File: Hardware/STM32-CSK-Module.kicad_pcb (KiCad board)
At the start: 2 copper layers, 32 parts, among them J1 Conn_Cortex-JTAG-10, U1 STM32F417VGT, X1 8MHz, X2 32.768kHz

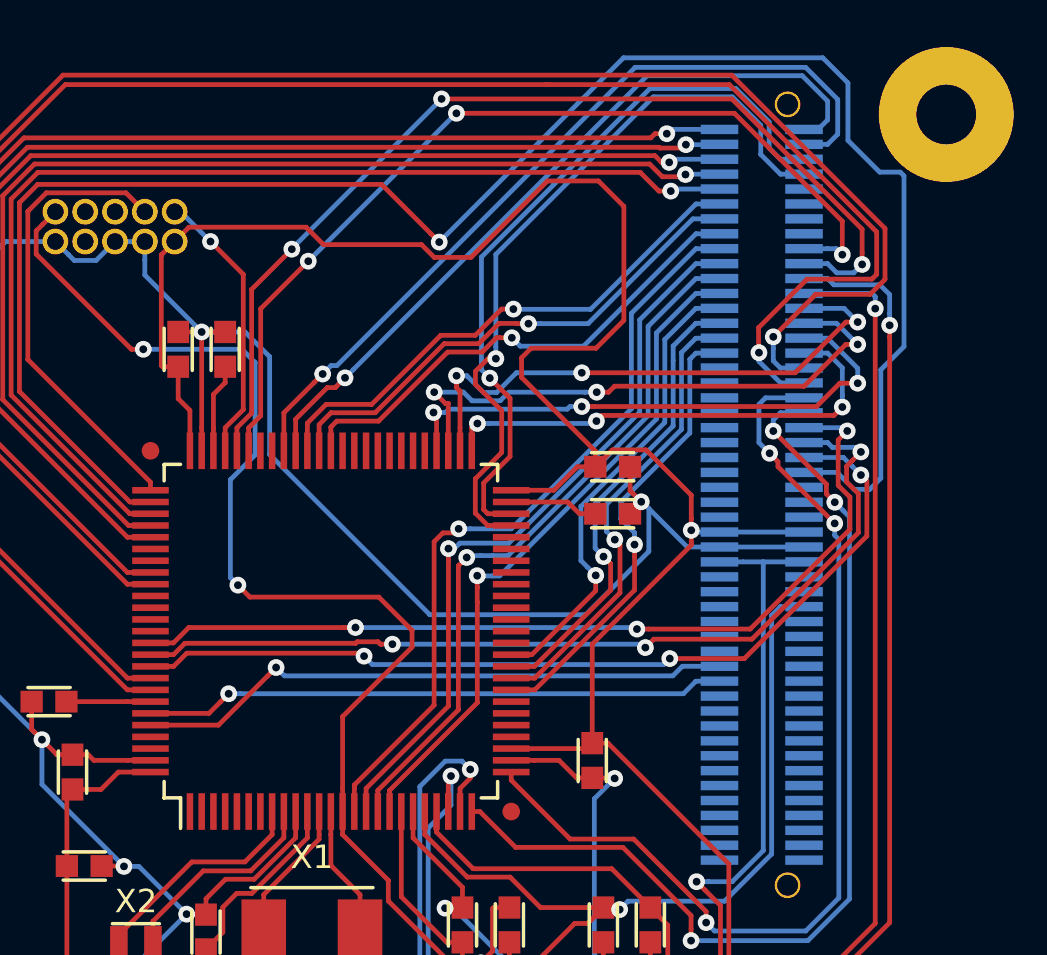
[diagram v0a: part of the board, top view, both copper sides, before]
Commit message: Finished all H1 GPIO
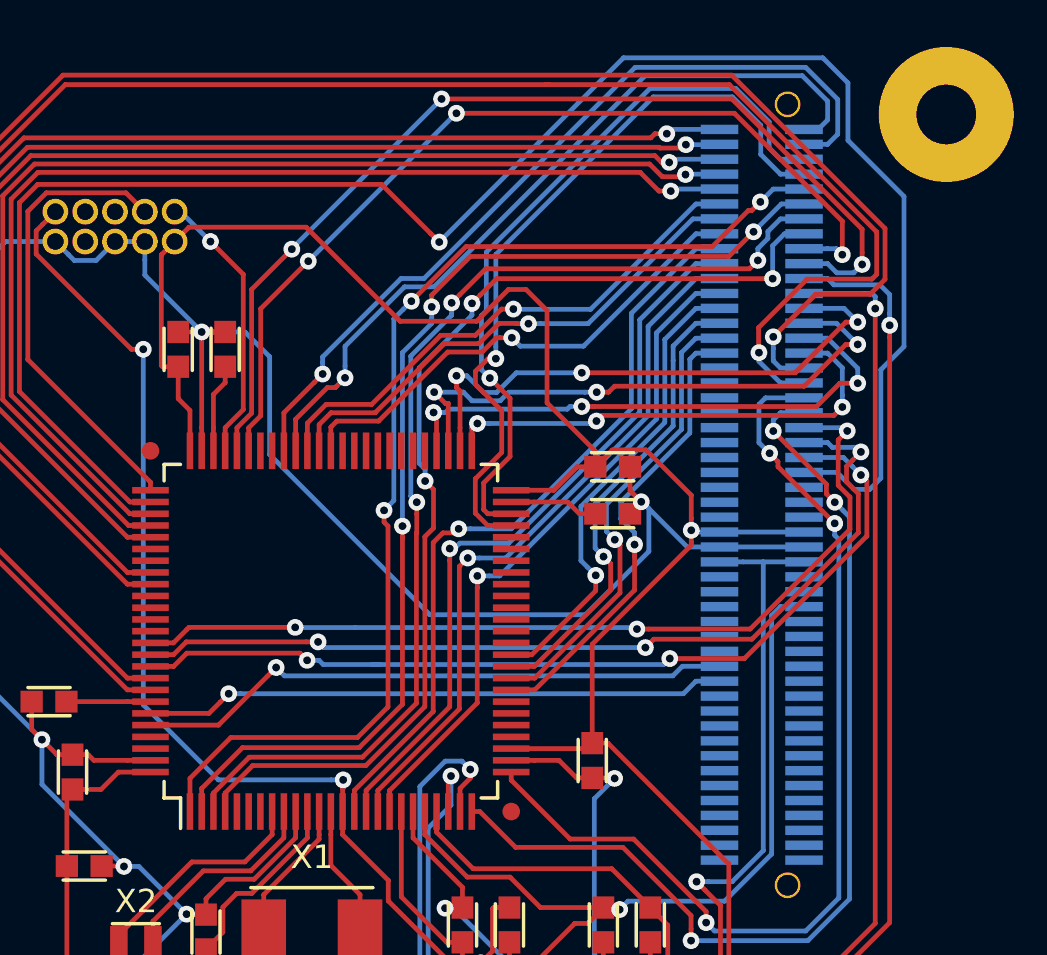
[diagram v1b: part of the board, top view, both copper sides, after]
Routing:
- net /IO19: track 0.00 -> 47.6 mm, vias 0 -> 3
- net /IO18: track 0.00 -> 46.4 mm, vias 0 -> 3
- net /IO17: track 0.00 -> 45.9 mm, vias 0 -> 3
- net /IO16: track 0.00 -> 45.5 mm, vias 0 -> 3
- net +3V3: track 159.9 -> 148.6 mm
- net /~RST: track 53.8 -> 48.0 mm
- net /I2C3_SDA: track 32.5 -> 33.3 mm
- net /~SPI1_SS: track 78.4 -> 77.9 mm

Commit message: Done. Moderately clean.
All used pins routed.
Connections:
- H1 pad 33: Net-(H1-Pad33) -> /IO31
- H1 pad 35: Net-(H1-Pad35) -> /IO30
- H1 pad 37: Net-(H1-Pad37) -> /IO29
- H1 pad 39: Net-(H1-Pad39) -> /IO28
- H1 pad 41: Net-(H1-Pad41) -> /IO27
- H1 pad 43: Net-(H1-Pad43) -> /IO26
- H1 pad 45: Net-(H1-Pad45) -> /IO25
- H1 pad 47: Net-(H1-Pad47) -> /IO24
- U1 pad 29: Net-(U1-Pad29) -> /IO28
- U1 pad 30: Net-(U1-Pad30) -> /IO29
- U1 pad 31: Net-(U1-Pad31) -> /IO30
- U1 pad 32: Net-(U1-Pad32) -> /IO31
- U1 pad 68: Net-(U1-Pad68) -> /IO27
- U1 pad 69: Net-(U1-Pad69) -> /IO26
- U1 pad 97: Net-(U1-Pad97) -> /IO24
- U1 pad 98: Net-(U1-Pad98) -> /IO25
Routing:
- net /IO26: track 0.00 -> 43.4 mm, vias 0 -> 3
- net /IO27: track 0.00 -> 40.5 mm, vias 0 -> 3
- net /IO25: track 0.00 -> 39.2 mm, vias 0 -> 3
- net /IO24: track 0.00 -> 37.0 mm, vias 0 -> 3
- net /IO28: track 0.00 -> 19.5 mm, vias 0 -> 1
- net /IO30: track 0.00 -> 19.4 mm, vias 0 -> 1
- net /IO31: track 0.00 -> 19.4 mm, vias 0 -> 1
- net /IO29: track 0.00 -> 19.0 mm, vias 0 -> 1
- net /SPI1_SCK: track 38.3 -> 46.8 mm
- net /SPI1_MISO: track 39.0 -> 46.5 mm
- net /SPI1_MOSI: track 38.9 -> 46.2 mm
- net +3V3: track 148.6 -> 151.1 mm
- net /USART1_RX: track 80.0 -> 82.2 mm
- net /USART1_TX: track 79.7 -> 81.4 mm
- net /~SPI1_SS: track 77.9 -> 79.4 mm
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
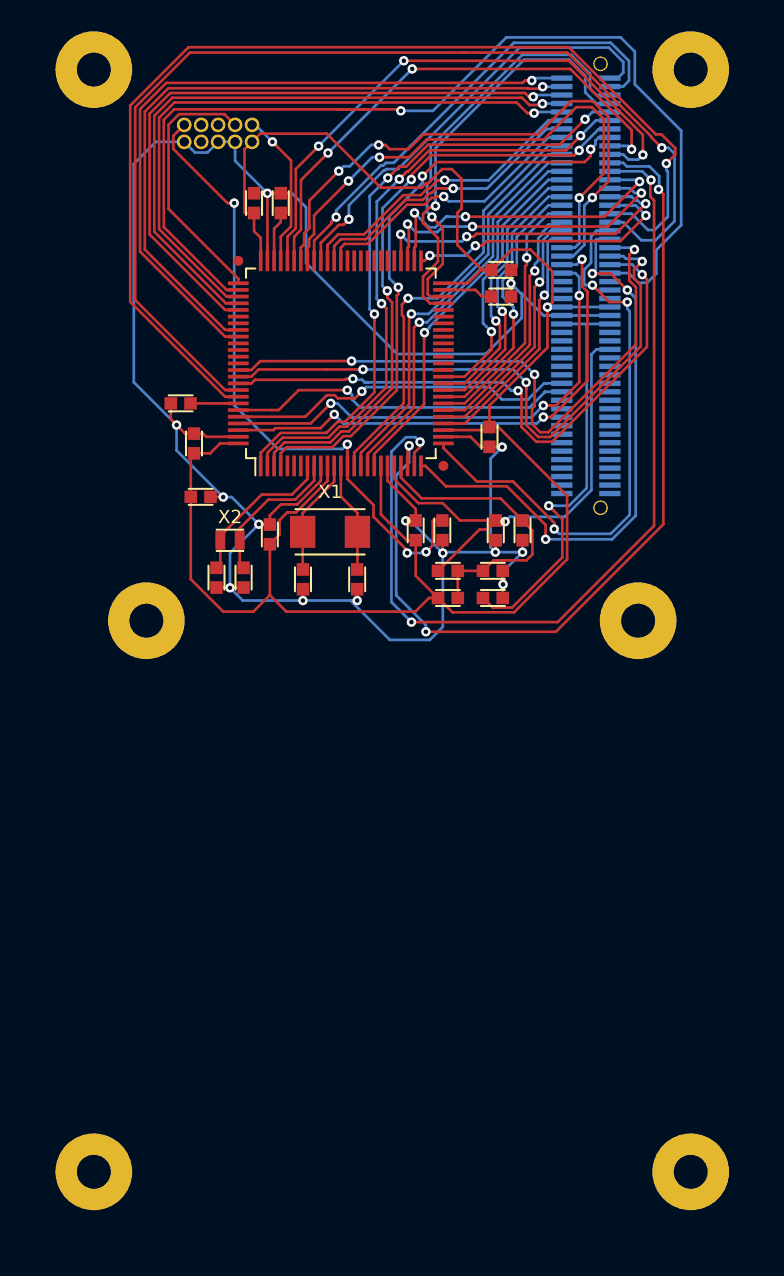
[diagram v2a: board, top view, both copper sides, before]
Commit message: Created ground plane
Large parts of ground plane unconnected. Not surprising given the density
of traces in most parts.
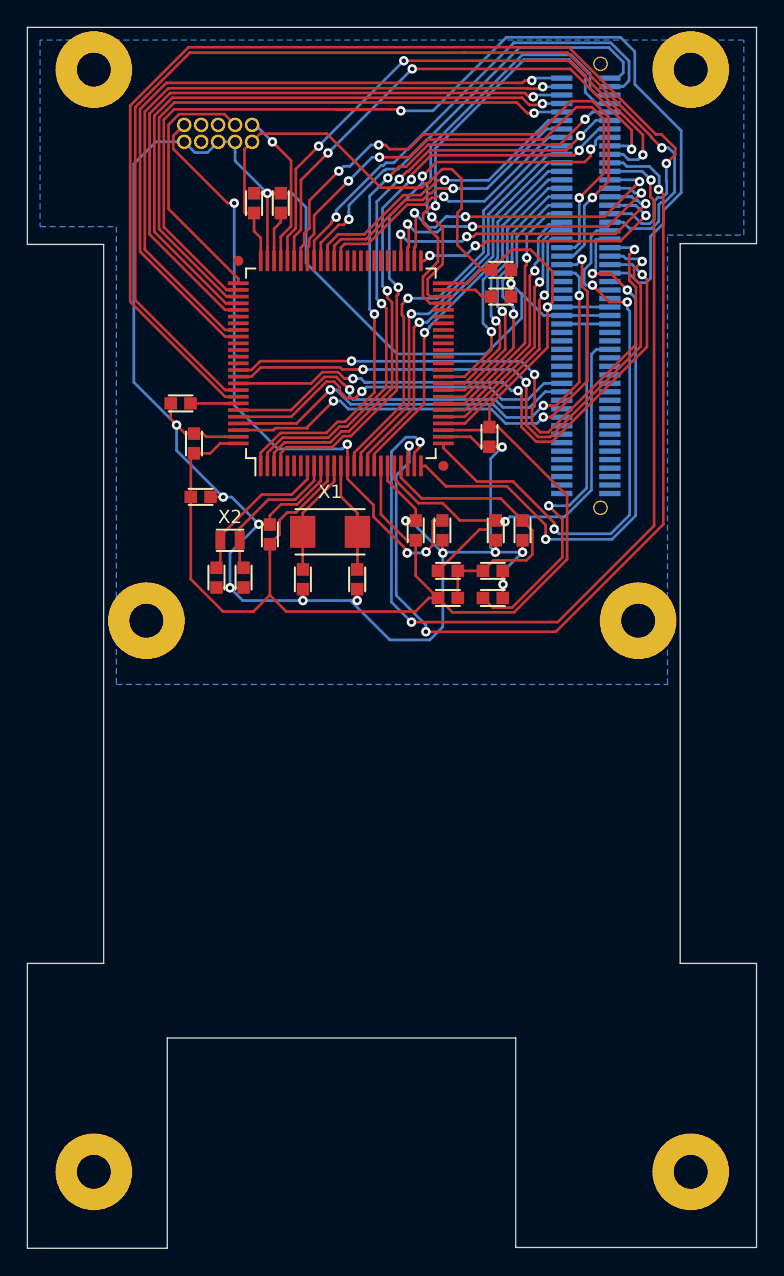
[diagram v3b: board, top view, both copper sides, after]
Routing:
- net /USART1_TX: track 81.4 -> 80.1 mm
- net /I2C1_SDA: track 26.2 -> 27.2 mm
- net /I2C1_SCL: track 26.1 -> 27.0 mm
- net /IO25: track 39.2 -> 40.1 mm
- net /IO24: track 37.0 -> 37.8 mm
- net /USART1_RX: track 82.2 -> 81.5 mm
- added copper zone on B.Cu, net GND
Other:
- board outline added: 54.6 x 91.4 mm

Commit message: FUCK FUCKING FUCK FUCK FUCK FUCK FUCKING FUCK FUCK
COCK
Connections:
- H1 pad 1: /IO47 -> /I2C3_SDA
- H1 pad 10: /IO19 -> /IO43
- H1 pad 11: /IO42 -> /IO18
- H1 pad 12: /IO18 -> /IO42
- H1 pad 13: /IO41 -> /IO17
- H1 pad 14: /IO17 -> /IO41
- H1 pad 15: /IO40 -> /IO16
- H1 pad 16: /IO16 -> /IO40
- H1 pad 17: /AN2 -> /USART1_CTS
- H1 pad 18: /USART1_CTS -> /AN2
- H1 pad 19: /AN3 -> /USART1_RTS
- H1 pad 2: /I2C3_SDA -> /IO47
- H1 pad 20: /USART1_RTS -> /AN3
- H1 pad 21: /AN4 -> /USART2_CTS
- H1 pad 22: /USART2_CTS -> /AN4
- H1 pad 23: /AN5 -> /USART2_RTS
- H1 pad 24: /USART2_RTS -> /AN5
- H1 pad 25: /AN1 -> /SPI2_SCK
- H1 pad 26: /SPI2_SCK -> /AN1
- H1 pad 27: /AN0 -> /SPI2_MISO
- H1 pad 28: /SPI2_MISO -> /AN0
- H1 pad 29: /AN7 -> /SPI2_MOSI
- H1 pad 3: /IO46 -> /I2C3_SCL
- H1 pad 30: /SPI2_MOSI -> /AN7
- H1 pad 31: /AN6 -> /~SPI2_SS
- H1 pad 32: /~SPI2_SS -> /AN6
- H1 pad 33: /IO31 -> /USART1_RX
- H1 pad 34: /USART1_RX -> /IO31
- H1 pad 35: /IO30 -> /USART1_TX
- H1 pad 36: /USART1_TX -> /IO30
- H1 pad 37: /IO29 -> /USART2_RX
- H1 pad 38: /USART2_RX -> /IO29
- H1 pad 39: /IO28 -> /USART2_TX
- H1 pad 4: /I2C3_SCL -> /IO46
- H1 pad 40: /USART2_TX -> /IO28
- H1 pad 41: /IO27 -> /SPI1_SCK
- H1 pad 42: /SPI1_SCK -> /IO27
- H1 pad 43: /IO26 -> /SPI1_MISO
- H1 pad 44: /SPI1_MISO -> /IO26
- H1 pad 45: /IO25 -> /SPI1_MOSI
- H1 pad 46: /SPI1_MOSI -> /IO25
- H1 pad 47: /IO24 -> /~SPI1_SS
- H1 pad 48: /~SPI1_SS -> /IO24
- H1 pad 5: /IO45 -> /I2C2_SDA
- H1 pad 6: /I2C2_SDA -> /IO45
- H1 pad 65: Net-(H1-Pad65) -> /VREF
- H1 pad 66: /VREF -> Net-(H1-Pad66)
- H1 pad 69: /~RESET -> Net-(H1-Pad69)
- H1 pad 7: /IO44 -> /I2C2_SCL
- H1 pad 70: Net-(H1-Pad70) -> /~RESET
- H1 pad 73: /I2C1_SDA -> Net-(H1-Pad73)
- H1 pad 74: Net-(H1-Pad74) -> /I2C1_SDA
- H1 pad 75: /I2C1_SCL -> Net-(H1-Pad75)
- H1 pad 76: Net-(H1-Pad76) -> /I2C1_SCL
- H1 pad 8: /I2C2_SCL -> /IO44
- H1 pad 81: Net-(H1-Pad81) -> /~ON_SD
- H1 pad 82: /~ON_SD -> Net-(H1-Pad82)
- H1 pad 9: /IO43 -> /IO19
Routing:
- net /USART1_RX: track 81.5 -> 0.00 mm, vias 1 -> 0
- net /USART1_TX: track 80.1 -> 0.26 mm, vias 1 -> 0
- net /~SPI1_SS: track 79.4 -> 0.00 mm, vias 1 -> 0
- net /USART2_RTS: track 68.6 -> 0.00 mm, vias 3 -> 0
- net /USART2_CTS: track 68.3 -> 0.00 mm, vias 3 -> 0
- net /IO47: track 53.2 -> 0.60 mm, vias 1 -> 0
- net /IO46: track 51.9 -> 0.00 mm, vias 1 -> 0
- net /IO45: track 49.7 -> 0.00 mm, vias 1 -> 0
- net /IO44: track 48.5 -> 0.00 mm, vias 1 -> 0
- net /IO43: track 47.4 -> 0.00 mm, vias 1 -> 0
- net /SPI1_SCK: track 46.8 -> 0.00 mm, vias 3 -> 0
- net /IO19: track 46.8 -> 0.00 mm, vias 3 -> 0
- net /SPI1_MISO: track 46.7 -> 0.00 mm, vias 3 -> 0
- net /SPI1_MOSI: track 46.6 -> 0.00 mm, vias 3 -> 0
- net /IO18: track 46.1 -> 0.00 mm, vias 3 -> 0
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
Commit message: Restarted with the connector NOT FUCKING WRONG!
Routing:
- net /IO27: track 0.03 -> 52.4 mm, vias 0 -> 3
- net /IO26: track 0.00 -> 52.2 mm, vias 0 -> 3
- net /USART1_RX: track 0.00 -> 39.7 mm, vias 0 -> 1
- net /USART1_TX: track 0.26 -> 37.5 mm, vias 0 -> 1
- net /USART2_TX: track 0.00 -> 34.7 mm, vias 0 -> 1
- net /USART2_RX: track 0.00 -> 34.5 mm, vias 0 -> 1
- net /I2C1_SDA: track 0.00 -> 33.7 mm, vias 0 -> 3
- net /I2C1_SCL: track 0.00 -> 31.3 mm, vias 0 -> 3
- net /SPI1_SCK: track 0.00 -> 28.0 mm, vias 0 -> 1
- net /SPI1_MISO: track 0.00 -> 28.0 mm, vias 0 -> 1
- net /SPI1_MOSI: track 0.00 -> 27.9 mm, vias 0 -> 1
- net /AN6: track 0.00 -> 27.2 mm, vias 0 -> 1
- net /~SPI1_SS: track 0.00 -> 26.6 mm, vias 0 -> 1
- net /AN7: track 0.00 -> 25.8 mm, vias 0 -> 1
- net /IO31: track 0.00 -> 25.5 mm, vias 0 -> 1
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
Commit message: Done routing it properly
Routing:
- net /IO16: track 0.00 -> 81.8 mm, vias 0 -> 1
- net /IO17: track 0.00 -> 77.4 mm, vias 0 -> 1
- net /IO18: track 0.00 -> 72.5 mm, vias 0 -> 1
- net /IO19: track 0.00 -> 68.0 mm, vias 0 -> 1
- net /IO47: track 0.60 -> 62.6 mm, vias 0 -> 1
- net /IO46: track 0.00 -> 60.2 mm, vias 0 -> 1
- net /IO45: track 0.00 -> 58.7 mm, vias 0 -> 1
- net /IO44: track 0.00 -> 57.6 mm, vias 0 -> 1
- net /IO25: track 0.00 -> 56.0 mm, vias 0 -> 3
- net /IO43: track 0.00 -> 54.9 mm, vias 0 -> 1
- net /AN2: track 0.00 -> 53.2 mm, vias 0 -> 3
- net /IO24: track 0.00 -> 52.8 mm, vias 0 -> 3
- net /AN3: track 0.00 -> 49.5 mm, vias 0 -> 3
- net /AN4: track 0.00 -> 45.5 mm, vias 0 -> 3
- net /AN5: track 0.00 -> 43.3 mm, vias 0 -> 3
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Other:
- board size 54.6 x 91.4 mm -> 54.6 x 50.5 mm
